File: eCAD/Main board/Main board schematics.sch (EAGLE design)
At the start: 17 parts, among them IC1 ESP32-WROOM-32E__8MB_, Q1 IRF7319TRPBF, Q2 IRF7319TRPBF

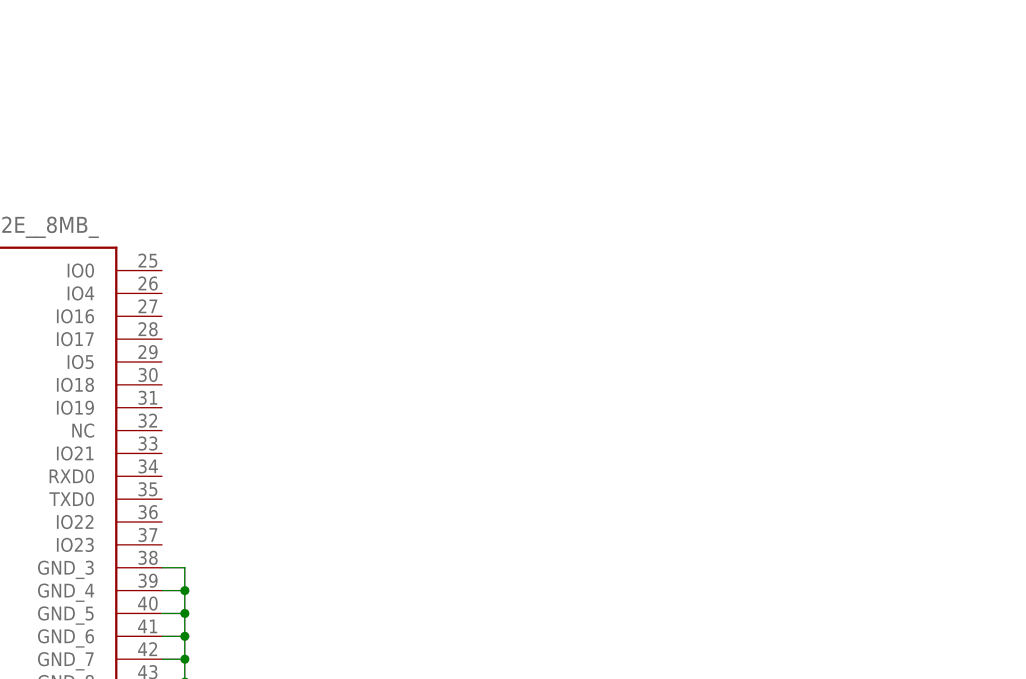
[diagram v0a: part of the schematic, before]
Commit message: Added uart programming interface
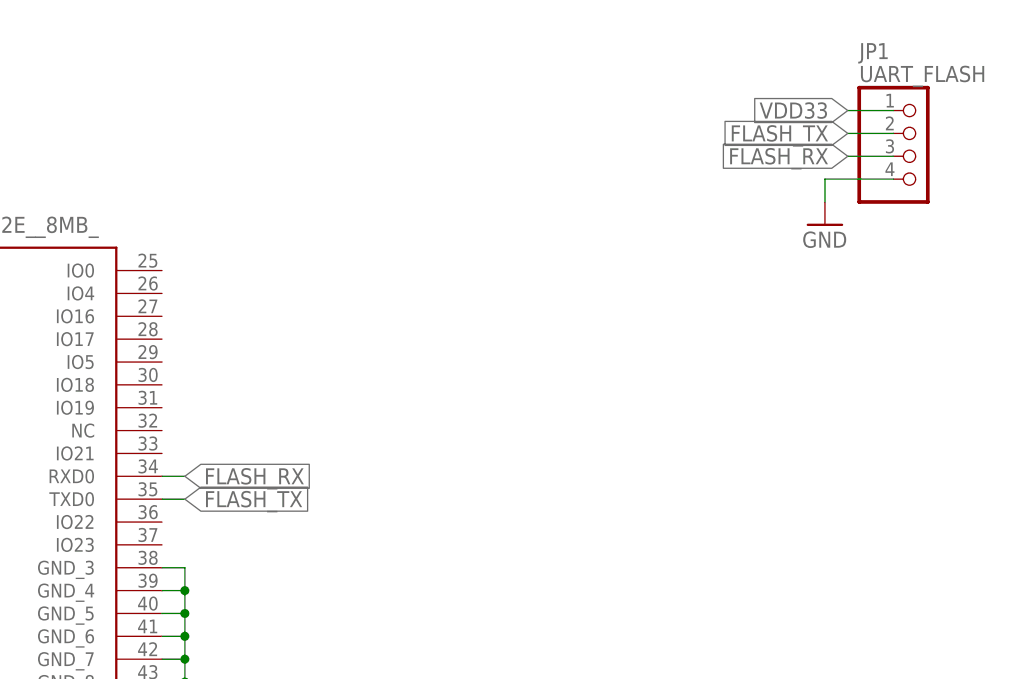
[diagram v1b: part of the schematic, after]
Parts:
- added JP1: UART_FLASH, pinhead:PINHD-1X4
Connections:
- new net FLASH_RX: IC1.RXD0, JP1.3
- new net FLASH_TX: IC1.TXD0, JP1.2
- net GND: now also JP1.4
- net VDD33: now also JP1.1
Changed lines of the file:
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@@
 <grid distance="0.1" unitdist="inch" unit="inch" style="lines" multiple="1" display="yes" altdistance="0.01" altunitdist="inch" altunit="inch"/>
 <layers>
-<layer number="1" name="Top" color="4" fill="1" visible="yes" active="no"/>
-<layer number="2" name="Route2" color="1" fill="3" visible="yes" active="no"/>
-<layer number="3" name="Route3" color="4" fill="3" visible="yes" active="no"/>
-<layer number="4" name="Route4" color="1" fill="4" visible="yes" active="no"/>
-<layer number="5" name="Route5" color="4" fill="4" visible="yes" active="no"/>
-<layer number="6" name="Route6" color="1" fill="8" visible="yes" active="no"/>
-<layer number="7" name="Route7" color="4" fill="8" visible="yes" active="no"/>
-<layer number="8" name="Route8" color="1" fill="2" visible="yes" active="no"/>
-<layer number="9" name="Route9" color="4" fill="2" visible="yes" active="no"/>
-<layer number="10" name="Route10" color="1" fill="7" visible="yes" active="no"/>
-<layer number="11" name="Route11" color="4" fill="7" visible="yes" active="no"/>
-<layer number="12" name="Route12" color="1" fill="5" visible="yes" active="no"/>
-<layer number="13" name="Route13" color="4" fill="5" visible="yes" active="no"/>
-<layer number="14" name="Route14" color="1" fill="6" visible="yes" active="no"/>
-<layer number="15" name="Route15" color="4" fill="6" visible="yes" active="no"/>
-<layer number="16" name="Bottom" color="1" fill="1" visible="yes" active="no"/>
-<layer number="17" name="Pads" color="2" fill="1" visible="yes" active="no"/>
-<layer number="18" name="Vias" color="2" fill="1" visible="yes" active="no"/>
-<layer number="19" name="Unrouted" color="6" fill="1" visible="yes" active="no"/>
-<layer number="20" name="Dimension" color="15" fill="1" visible="yes" active="no"/>
-<layer number="21" name="tPlace" color="7" fill="1" visible="yes" active="no"/>
-<layer number="22" name="bPlace" color="7" fill="1" visible="yes" active="no"/>
-<layer number="23" name="tOrigins" color="15" fill="1" visible="yes" active="no"/>
-<layer number="24" name="bOrigins" color="15" fill="1" visible="yes" active="no"/>
-<layer number="25" name="tNames" color="7" fill="1" visible="yes" active="no"/>
-<layer number="26" name="bNames" color="7" fill="1" visible="yes" active="no"/>
-<layer number="27" name="tValues" color="7" fill="1" visible="yes" active="no"/>
-<layer number="28" name="bValues" color="7" fill="1" visible="yes" active="no"/>
+<layer number="1" name="Top" color="4" fill="1" visible="no" active="no"/>
+<layer number="2" name="Route2" color="1" fill="3" visible="no" active="no"/>
+<layer number="3" name="Route3" color="4" fill="3" visible="no" active="no"/>
+<layer number="4" name="Route4" color="1" fill="4" visible="no" active="no"/>
+<layer number="5" name="Route5" color="4" fill="4" visible="no" active="no"/>
+<layer number="6" name="Route6" color="1" fill="8" visible="no" active="no"/>
+<layer number="7" name="Route7" color="4" fill="8" visible="no" active="no"/>
+<layer number="8" name="Route8" color="1" fill="2" visible="no" active="no"/>
+<layer number="9" name="Route9" color="4" fill="2" visible="no" active="no"/>
+<layer number="10" name="Route10" color="1" fill="7" visible="no" active="no"/>
+<layer number="11" name="Route11" color="4" fill="7" visible="no" active="no"/>
+<layer number="12" name="Route12" color="1" fill="5" visible="no" active="no"/>
+<layer number="13" name="Route13" color="4" fill="5" visible="no" active="no"/>
+<layer number="14" name="Route14" color="1" fill="6" visible="no" active="no"/>
+<layer number="15" name="Route15" color="4" fill="6" visible="no" active="no"/>
+<layer number="16" name="Bottom" color="1" fill="1" visible="no" active="no"/>
+<layer number="17" name="Pads" color="2" fill="1" visible="no" active="no"/>
+<layer number="18" name="Vias" color="2" fill="1" visible="no" active="no"/>
+<layer number="19" name="Unrouted" color="6" fill="1" visible="no" active="no"/>
+<layer number="20" name="Dimension" color="15" fill="1" visible="no" active="no"/>
+<layer number="21" name="tPlace" color="7" fill="1" visible="no" active="no"/>
+<layer number="22" name="bPlace" color="7" fill="1" visible="no" active="no"/>
+<layer number="23" name="tOrigins" color="15" fill="1" visible="no" active="no"/>
+<layer number="24" name="bOrigins" color="15" fill="1" visible="no" active="no"/>
+<layer number="25" name="tNames" color="7" fill="1" visible="no" active="no"/>
+<layer number="26" name="bNames" color="7" fill="1" visible="no" active="no"/>
+<layer number="27" name="tValues" color="7" fill="1" visible="no" active="no"/>
+<layer number="28" name="bValues" color="7" fill="1" visible="no" active="no"/>
 <layer number="29" name="tStop" color="7" fill="3" visible="no" active="no"/>
 <layer number="30" name="bStop" color="7" fill="6" visible="no" active="no"/>
@@
 <layer number="35" name="tGlue" color="7" fill="4" visible="no" active="no"/>
 <layer number="36" name="bGlue" color="7" fill="5" visible="no" active="no"/>
-<layer number="37" name="tTest" color="7" fill="1" visible="yes" active="no"/>
-<layer number="38" name="bTest" color="7" fill="1" visible="yes" active="no"/>
+<layer number="37" name="tTest" color="7" fill="1" visible="no" active="no"/>
+<layer number="38" name="bTest" color="7" fill="1" visible="no" active="no"/>
 <layer number="39" name="tKeepout" color="4" fill="11" visible="no" active="no"/>
 <layer number="40" name="bKeepout" color="1" fill="11" visible="no" active="no"/>
@@
 <layer number="44" name="Drills" color="7" fill="1" visible="no" active="no"/>
 <layer number="45" name="Holes" color="7" fill="1" visible="no" active="no"/>
-<layer number="46" name="Milling" color="3" fill="1" visible="yes" active="no"/>
-<layer number="47" name="Measures" color="7" fill="1" visible="yes" active="no"/>
-<layer number="48" name="Document" color="7" fill="1" visible="yes" active="no"/>
-<layer number="49" name="Reference" color="7" fill="1" visible="yes" active="no"/>
-<layer number="51" name="tDocu" color="7" fill="1" visible="yes" active="no"/>
-<layer number="52" name="bDocu" color="7" fill="1" visible="yes" active="no"/>
+<layer number="46" name="Milling" color="3" fill="1" visible="no" active="no"/>
+<layer number="47" name="Measures" color="7" fill="1" visible="no" active="no"/>
+<layer number="48" name="Document" color="7" fill="1" visible="no" active="no"/>
+<layer number="49" name="Reference" color="7" fill="1" visible="no" active="no"/>
+<layer number="51" name="tDocu" color="7" fill="1" visible="no" active="no"/>
+<layer number="52" name="bDocu" color="7" fill="1" visible="no" active="no"/>
 <layer number="88" name="SimResults" color="9" fill="1" visible="yes" active="yes"/>
 <layer number="89" name="SimProbes" color="9" fill="1" visible="yes" active="yes"/>
@@
 <part name="GND8" library="supply1" library_urn="urn:adsk.eagle:library:371" deviceset="GND" device=""/>
 <part name="GND9" library="supply1" library_urn="urn:adsk.eagle:library:371" deviceset="GND" device=""/>
+<part name="JP1" library="pinhead" library_urn="urn:adsk.eagle:library:325" deviceset="PINHD-1X4" device="" package3d_urn="urn:adsk.eagle:package:22407/2" value="UART_FLASH"/>
+<part name="GND10" library="supply1" library_urn="urn:adsk.eagle:library:371" deviceset="GND" device=""/>
 </parts>
 <sheets>
@@
 <instance part="GND9" gate="1" x="96.52" y="53.34" smashed="yes">
 <attribute name="VALUE" x="93.98" y="50.8" size="1.778" layer="96"/>
+</instance>
+<instance part="JP1" gate="A" x="299.72" y="231.14" smashed="yes">
+<attribute name="NAME" x="293.37" y="241.935" size="1.778" layer="95"/>
+<attribute name="VALUE" x="293.37" y="239.395" size="1.778" layer="96"/>
+</instance>
+<instance part="GND10" gate="1" x="289.56" y="223.52" smashed="yes">
+<attribute name="VALUE" x="287.02" y="220.98" size="1.778" layer="96"/>
 </instance>
 </instances>
@@
 <label x="101.6" y="58.42" size="1.778" layer="95" xref="yes"/>
 </segment>
+<segment>
+<pinref part="JP1" gate="A" pin="4"/>
+<wire x1="297.18" y1="228.6" x2="289.56" y2="228.6" width="0.1524" layer="91"/>
+<wire x1="289.56" y1="228.6" x2="289.56" y2="226.06" width="0.1524" layer="91"/>
+<pinref part="GND10" gate="1" pin="GND"/>
+</segment>
 </net>
 <net name="ESP_EN" class="0">
@@
 <junction x="58.42" y="81.28"/>
 </segment>
+<segment>
+<pinref part="JP1" gate="A" pin="1"/>
+<wire x1="297.18" y1="236.22" x2="292.1" y2="236.22" width="0.1524" layer="91"/>
+<label x="292.1" y="236.22" size="1.778" layer="95" rot="R180" xref="yes"/>
+</segment>
 </net>
 <net name="ESP_PIN" class="0">
@@
 </segment>
 </net>
+<net name="FLASH_RX" class="0">
+<segment>
+<pinref part="IC1" gate="G$1" pin="RXD0"/>
+<wire x1="215.9" y1="195.58" x2="218.44" y2="195.58" width="0.1524" layer="91"/>
+<label x="218.44" y="195.58" size="1.778" layer="95" xref="yes"/>
+</segment>
+<segment>
+<pinref part="JP1" gate="A" pin="3"/>
+<wire x1="297.18" y1="231.14" x2="292.1" y2="231.14" width="0.1524" layer="91"/>
+<label x="292.1" y="231.14" size="1.778" layer="95" rot="R180" xref="yes"/>
+</segment>
+</net>
+<net name="FLASH_TX" class="0">
+<segment>
+<pinref part="IC1" gate="G$1" pin="TXD0"/>
+<wire x1="215.9" y1="193.04" x2="218.44" y2="193.04" width="0.1524" layer="91"/>
+<label x="218.44" y="193.04" size="1.778" layer="95" xref="yes"/>
+</segment>
+<segment>
+<pinref part="JP1" gate="A" pin="2"/>
+<wire x1="297.18" y1="233.68" x2="292.1" y2="233.68" width="0.1524" layer="91"/>
+<label x="292.1" y="233.68" size="1.778" layer="95" rot="R180" xref="yes"/>
+</segment>
+</net>

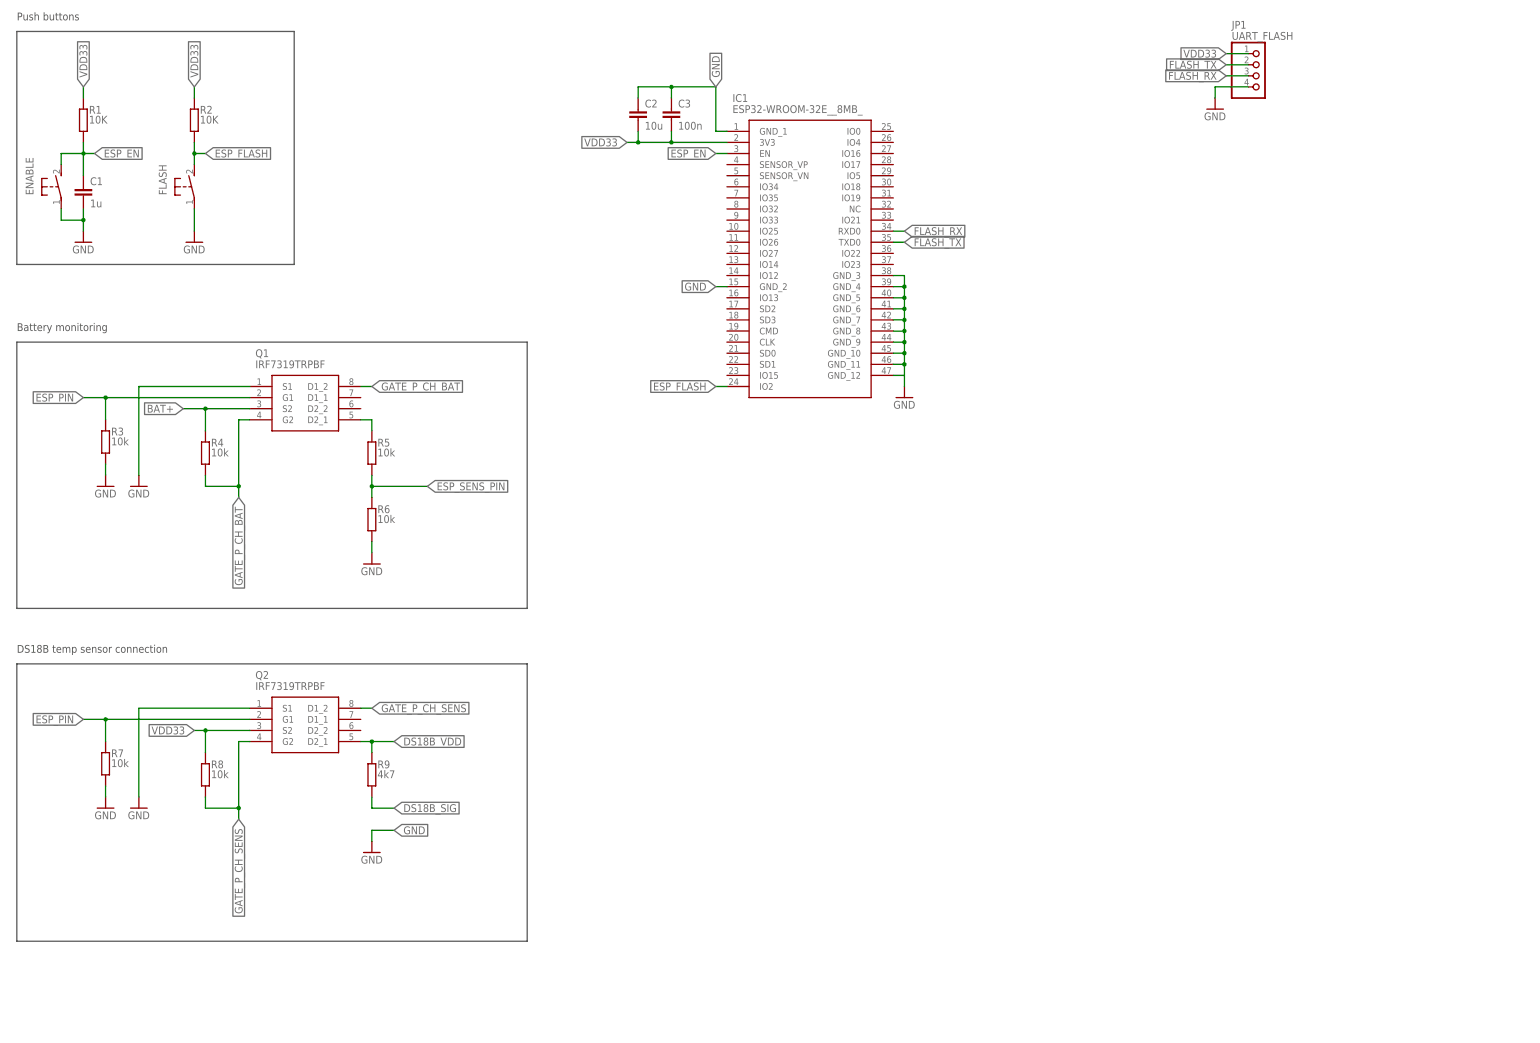
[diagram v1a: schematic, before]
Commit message: Added power circuits, connection to Quectel devkit
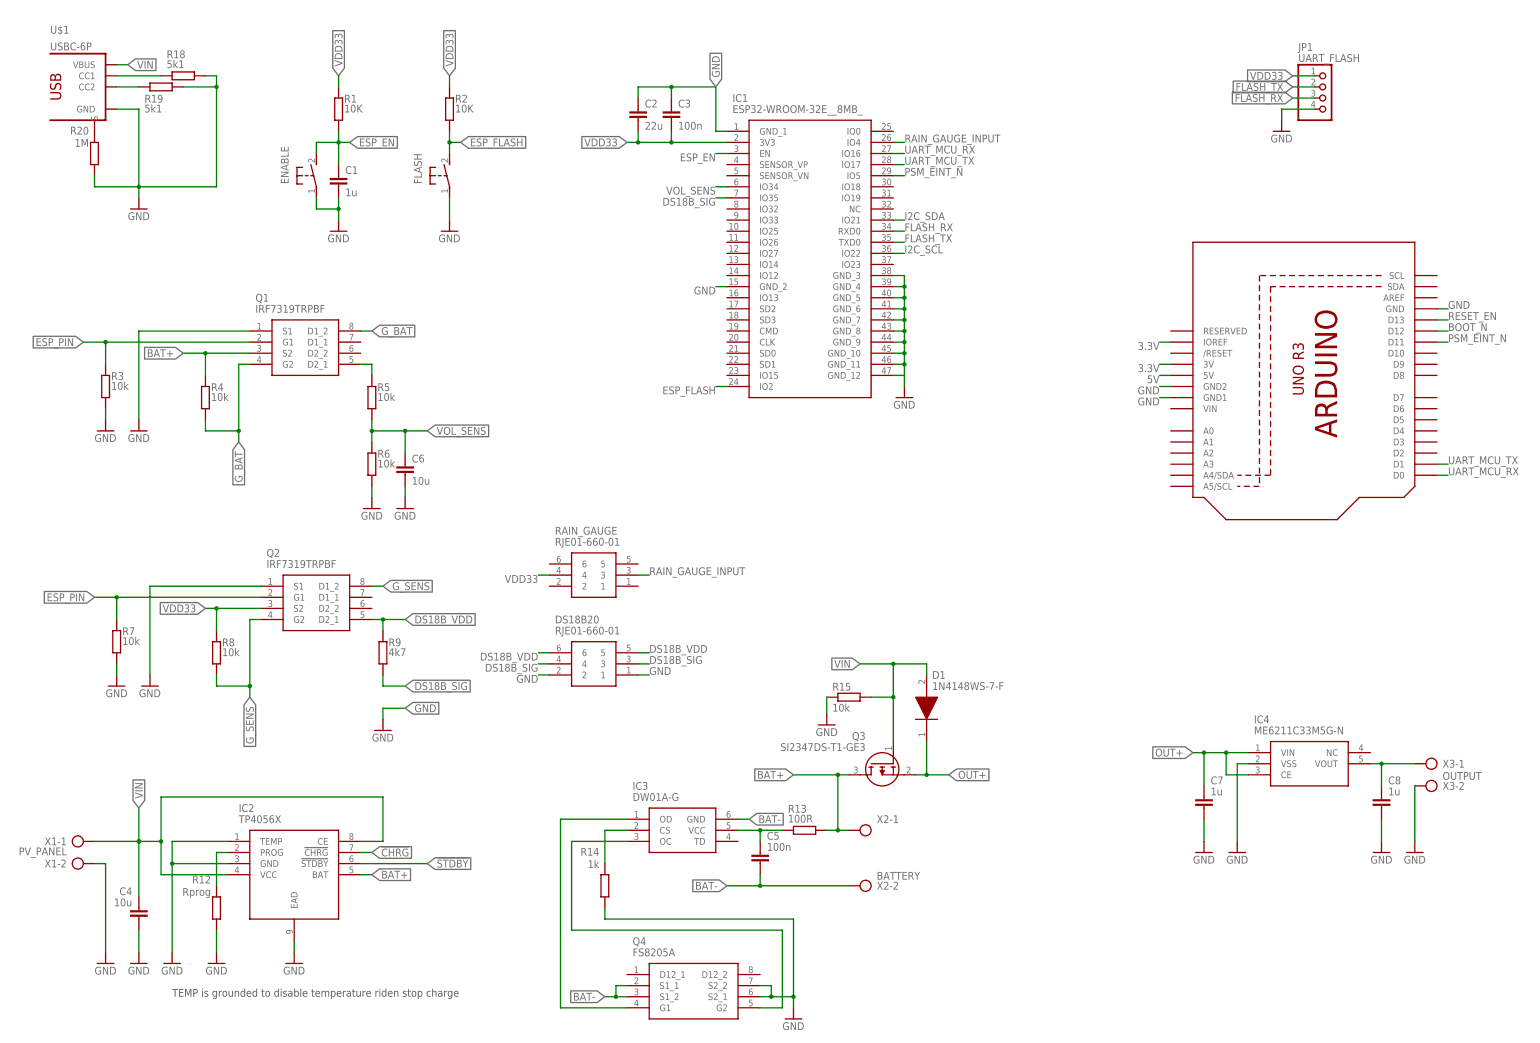
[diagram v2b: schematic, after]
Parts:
- added C4: 10u, rcl:C-EUC0805
- added C5: 100n, rcl:C-EUC0805
- added C6: 10u, rcl:C-EUC1206
- added C7, C8: 1u, rcl:C-EUC0805
- added D1: 1N4148WS-7-F, 1-component-search:1N4148WS-7-F
- added DS18B20, RAIN_GAUGE: RJE01-660-01, 1-component-search:RJE01-660-01
- added IC2: TP4056X, TP4056X:TP4056X
- added IC3: DW01A-G, 1-component-search:DW01A-G
- added IC4: ME6211C33M5G-N, 1-component-search:ME6211C33M5G-N
- added Q3: SI2347DS-T1-GE3, 1-component-search:SI2347DS-T1-GE3
- added Q4: FS8205A, 1-component-search:FS8205A
- added QUECTEL_BC660K-GL-TE-B_ARDUINO_INTERFACE: ARDUINOR3-BPLACE, adafruit:ARDUINOR3-BPLACE
- added R12: Rprog, rcl:R-EU_R0805
- added R13: 100R, rcl:R-EU_R0805
- added R14: 1k, rcl:R-EU_R0805
- added R15: 10k, rcl:R-EU_R0805
- added R18, R19: 5k1, rcl:R-EU_R0805
- added R20: 1M, rcl:R-EU_R0805
- added U$1: USBC-6P, USBC6P:USBC-6P
- added X1: PV_PANEL, con-ptr500:AK300/2
- added X2: BATTERY, con-ptr500:AK300/2
- added X3: OUTPUT, con-ptr500:AK300/2
- C2: value 10u -> 22u
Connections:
- net GATE_P_CH_BAT renamed G_BAT
- net GATE_P_CH_SENS renamed G_SENS
- removed net ESP_SENS_PIN: R5.1, R6.2
- new net !CHRG: IC2.!CHRG
- new net !STDBY: IC2.!STDBY
- new net 3.3V: QUECTEL_BC660K-GL-TE-B_ARDUINO_INTERFACE.3V, QUECTEL_BC660K-GL-TE-B_ARDUINO_INTERFACE.IOREF
- new net 5V: QUECTEL_BC660K-GL-TE-B_ARDUINO_INTERFACE.5V
- new net BAT-: C5.2, IC3.GND, Q4.S1_1, Q4.S1_2, X2-2.KL
- new net BOOT_N: QUECTEL_BC660K-GL-TE-B_ARDUINO_INTERFACE.D12
- new net I2C_SCL: IC1.IO22
- new net I2C_SDA: IC1.IO21
- new net N$10: IC3.OD, Q4.G1
- new net N$11: R19.2, U$1.CC2
- new net N$12: IC3.OC, Q4.G2
- new net N$13: R18.2, U$1.CC1
- new net N$14: C8.1, IC4.VOUT, X3-1.KL
- new net N$4: IC2.PROG, R12.1
- new net N$7: C5.1, IC3.VCC, R13.1
- new net N$8: R20.1, U$1.S
- new net N$9: IC3.CS, R14.2
- new net OUT+: C7.1, D1.K, IC4.CE, IC4.VIN, Q3.S
- new net PSM_EINT_N: IC1.IO5, QUECTEL_BC660K-GL-TE-B_ARDUINO_INTERFACE.D11
- new net RAIN_GAUGE_INPUT: IC1.IO4, RAIN_GAUGE.3
- new net RESET_EN: QUECTEL_BC660K-GL-TE-B_ARDUINO_INTERFACE.D13
- new net UART_MCU_RX: IC1.IO16, QUECTEL_BC660K-GL-TE-B_ARDUINO_INTERFACE.D0
- new net UART_MCU_TX: IC1.IO17, QUECTEL_BC660K-GL-TE-B_ARDUINO_INTERFACE.D1
- new net VIN: C4.1, D1.A, IC2.CE, IC2.VCC, Q3.G, R15.2, U$1.VBUS, X1-1.KL
- new net VOL_SENS: C6.1, IC1.IO34, R5.1, R6.2
- net BAT+: now also IC2.BAT, Q3.D, R13.2, X2-1.KL
- net DS18B_SIG: now also DS18B20.3, DS18B20.4, IC1.IO35
- net DS18B_VDD: now also DS18B20.5, DS18B20.6
- net GND: now also C4.2, C6.2, C7.2, C8.2, DS18B20.1, DS18B20.2, IC2.EAD, IC2.GND, IC2.TEMP, IC4.VSS, Q4.S2_1, Q4.S2_2, QUECTEL_BC660K-GL-TE-B_ARDUINO_INTERFACE.GND, QUECTEL_BC660K-GL-TE-B_ARDUINO_INTERFACE.GND1, QUECTEL_BC660K-GL-TE-B_ARDUINO_INTERFACE.GND2, R12.2, R14.1, R15.1, R18.1, R19.1, R20.2, U$1.GND, X1-2.KL, X3-2.KL
- net VDD33: now also RAIN_GAUGE.4
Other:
- note added: "TEMP is grounded to disable temperature riden stop charge"
- note removed: "Battery monitoring"
- note removed: "DS18B temp sensor connection"
- note removed: "Push buttons"
- moved on the sheet: C1, ENABLE, FLASH, JP1, Q1, Q2, R1, R2, R3, R4, R5, R6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
